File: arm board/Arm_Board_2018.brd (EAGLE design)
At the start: 193.8 x 103.9 mm, 165 parts, among them J1 RJ45KEYSTONE-942, J10 APP_2POS_CONFIGGENERAL_CONFIG, J11 APP_2POS_CONFIGGENERAL_CONFIG, J12 APP_2POS_CONFIGGENERAL_CONFIG, J13 APP_2POS_CONFIGGENERAL_CONFIG, J14 SL02, J15 SL02, J16 SL02, J2 JTAG_ARM_10PIN, J4 SL02, J5 APP_2POS_CONFIGGENERAL_CONFIG, J6 APP_2POS_CONFIGGENERAL_CONFIG, J7 APP_2POS_CONFIGGENERAL_CONFIG, J9 APP_2POS_CONFIGGENERAL_CONFIG, Q1 Q_IRF7437SMD, U1 TM4C1294NCPDT, U2 HX1198FNL, U3 SLVU2.8-4, Y1 NX3225GA, Y2 CRYATL_32K_SMD

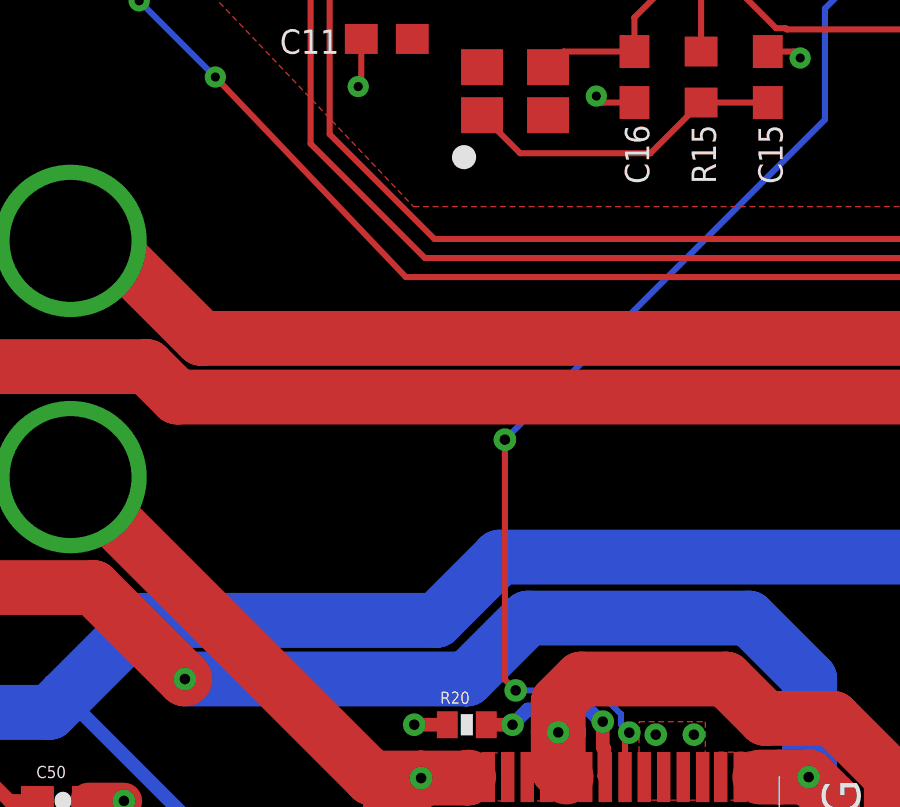
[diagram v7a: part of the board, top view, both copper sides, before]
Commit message: Connected the 3V3 plane to Logic 3.3V input
Fixed the fact that the tiva would not have any power without connecting
to the logic line.
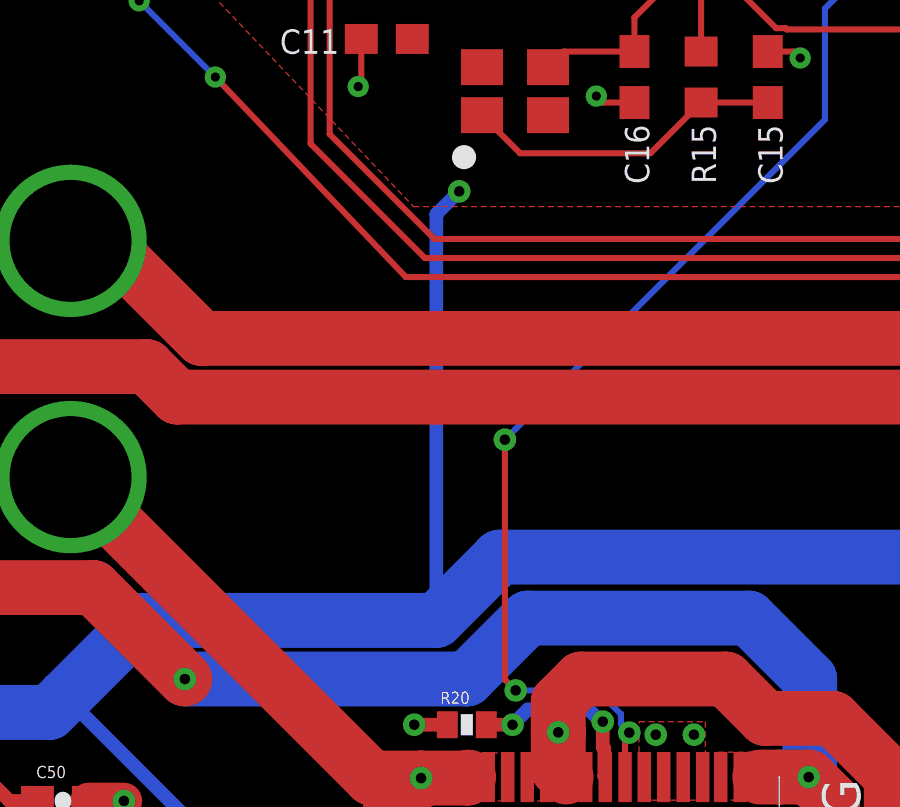
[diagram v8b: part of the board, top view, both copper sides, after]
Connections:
- removed net +3V3: C1.1, C10.1, C11.1, C2.1, C3.1, C4.1, C8.1, C9.1, J2.P1, LED3.A, R1.1, R12.2, R13.2, R17.1, R2.1, R3.1, R4.1, U1.P$101, U1.P$113, U1.P$122, U1.P$16, U1.P$26, U1.P$28, U1.P$39, U1.P$47, U1.P$51, U1.P$52, U1.P$69, U1.P$7, U1.P$79, U1.P$8, U1.P$9, U1.P$90, U2.P$2, U2.P$7
- net LOGIC_3.3V: now also C1.1, C10.1, C11.1, C2.1, C3.1, C4.1, C8.1, C9.1, J2.P1, LED3.A, R1.1, R12.2, R13.2, R17.1, R2.1, R3.1, R4.1, U1.P$101, U1.P$113, U1.P$122, U1.P$16, U1.P$26, U1.P$28, U1.P$39, U1.P$47, U1.P$51, U1.P$52, U1.P$69, U1.P$7, U1.P$79, U1.P$8, U1.P$9, U1.P$90, U2.P$2, U2.P$7
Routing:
- net LOGIC_3.3V: track 547.7 -> 569.0 mm, vias 14 -> 15
- net +3V3: track 9.27 -> 2.54 mm
- added copper zone on layer 1, net LOGIC_3.3V
- removed copper zone on layer 1, net +3V3
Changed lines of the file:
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@@
 <signals>
 <signal name="+3V3">
-<contactref element="U2" pad="P$2"/>
-<contactref element="C1" pad="1"/>
-<contactref element="R1" pad="1"/>
-<contactref element="R2" pad="1"/>
-<contactref element="R3" pad="1"/>
-<contactref element="R4" pad="1"/>
-<contactref element="C2" pad="1"/>
-<contactref element="C3" pad="1"/>
-<contactref element="R12" pad="2"/>
-<contactref element="R13" pad="2"/>
-<contactref element="U1" pad="P$9"/>
-<contactref element="U1" pad="P$7"/>
-<contactref element="U1" pad="P$122"/>
-<contactref element="U1" pad="P$113"/>
-<contactref element="U1" pad="P$101"/>
-<contactref element="U1" pad="P$90"/>
-<contactref element="U1" pad="P$79"/>
-<contactref element="U1" pad="P$69"/>
-<contactref element="U1" pad="P$52"/>
-<contactref element="U1" pad="P$51"/>
-<contactref element="U1" pad="P$47"/>
-<contactref element="U1" pad="P$39"/>
-<contactref element="U1" pad="P$28"/>
-<contactref element="U1" pad="P$26"/>
-<contactref element="U1" pad="P$16"/>
-<contactref element="U1" pad="P$8"/>
-<contactref element="C8" pad="1"/>
-<contactref element="C9" pad="1"/>
-<contactref element="C10" pad="1"/>
-<contactref element="C11" pad="1"/>
-<contactref element="R17" pad="1"/>
-<contactref element="J2" pad="P1"/>
-<polygon width="0.2032" layer="1">
-<vertex x="35.052" y="79.248"/>
-<vertex x="35.052" y="69.977"/>
-<vertex x="28.067" y="63.246"/>
-<vertex x="28.067" y="51.181"/>
-<vertex x="37.846" y="40.894"/>
-<vertex x="66.802" y="40.894"/>
-<vertex x="66.548" y="70.612"/>
-<vertex x="59.944" y="79.248"/>
-</polygon>
-<contactref element="C4" pad="1"/>
-<contactref element="U2" pad="P$7"/>
 <via x="46.482" y="68.707" extent="1-16" drill="0.3048"/>
 <via x="43.942" y="68.707" extent="1-16" drill="0.3048"/>
 <wire x1="43.942" y1="68.707" x2="46.482" y2="68.707" width="0.2032" layer="16"/>
-<contactref element="LED3" pad="A"/>
-<wire x1="46.97603125" y1="64.128953125" x2="46.97603125" y2="64.08546875" width="0.2032" layer="1"/>
-<wire x1="46.97603125" y1="64.08546875" x2="47.752" y2="63.3095" width="0.2032" layer="1"/>
-<wire x1="60.72925625" y1="62.714740625" x2="60.809740625" y2="62.714740625" width="0.2032" layer="1"/>
-<wire x1="60.809740625" y1="62.714740625" x2="61.722" y2="63.627" width="0.2032" layer="1"/>
-<wire x1="60.809740625" y1="62.714740625" x2="59.817" y2="61.722" width="0.2032" layer="1"/>
-<wire x1="66.968" y1="72.898" x2="64.516" y2="72.898" width="0.2032" layer="1"/>
-<wire x1="64.516" y1="72.898" x2="64.262" y2="72.644" width="0.2032" layer="1"/>
 </signal>
 <signal name="GND">
@@
 <via x="65.024" y="30.734" extent="1-16" drill="0.35"/>
 <wire x1="70.866" y1="23.114" x2="65.024" y2="28.956" width="0.4572" layer="1"/>
+<wire x1="38.608" y1="27.1018" x2="38.608" y2="40.64" width="0.4572" layer="16"/>
+<wire x1="38.608" y1="40.64" x2="39.37" y2="41.402" width="0.4572" layer="16"/>
+<via x="39.37" y="41.402" extent="1-16" drill="0.35"/>
+<contactref element="R12" pad="2"/>
+<contactref element="R13" pad="2"/>
+<contactref element="U1" pad="P$9"/>
+<contactref element="U1" pad="P$7"/>
+<contactref element="U1" pad="P$122"/>
+<contactref element="U1" pad="P$113"/>
+<contactref element="U1" pad="P$101"/>
+<contactref element="U1" pad="P$90"/>
+<contactref element="U1" pad="P$79"/>
+<contactref element="U1" pad="P$69"/>
+<contactref element="U1" pad="P$52"/>
+<contactref element="U1" pad="P$51"/>
+<contactref element="U1" pad="P$47"/>
+<contactref element="U1" pad="P$39"/>
+<contactref element="U1" pad="P$28"/>
+<contactref element="U1" pad="P$26"/>
+<contactref element="U1" pad="P$16"/>
+<contactref element="U1" pad="P$8"/>
+<contactref element="C8" pad="1"/>
+<contactref element="C9" pad="1"/>
+<contactref element="C10" pad="1"/>
+<contactref element="C11" pad="1"/>
+<wire x1="46.97603125" y1="64.128953125" x2="46.97603125" y2="64.08546875" width="0.2032" layer="1"/>
+<wire x1="46.97603125" y1="64.08546875" x2="47.752" y2="63.3095" width="0.2032" layer="1"/>
+<wire x1="60.72925625" y1="62.714740625" x2="60.809740625" y2="62.714740625" width="0.2032" layer="1"/>
+<wire x1="60.809740625" y1="62.714740625" x2="61.722" y2="63.627" width="0.2032" layer="1"/>
+<wire x1="60.809740625" y1="62.714740625" x2="59.817" y2="61.722" width="0.2032" layer="1"/>
+<wire x1="66.968" y1="72.898" x2="64.516" y2="72.898" width="0.2032" layer="1"/>
+<wire x1="64.516" y1="72.898" x2="64.262" y2="72.644" width="0.2032" layer="1"/>
+<contactref element="R17" pad="1"/>
+<contactref element="LED3" pad="A"/>
+<contactref element="J2" pad="P1"/>
+<contactref element="U2" pad="P$2"/>
+<contactref element="C1" pad="1"/>
+<contactref element="R1" pad="1"/>
+<contactref element="R2" pad="1"/>
+<contactref element="R3" pad="1"/>
+<contactref element="R4" pad="1"/>
+<contactref element="C2" pad="1"/>
+<contactref element="C3" pad="1"/>
+<contactref element="C4" pad="1"/>
+<contactref element="U2" pad="P$7"/>
+<polygon width="0.2032" layer="1">
+<vertex x="35.052" y="79.248"/>
+<vertex x="35.052" y="69.977"/>
+<vertex x="28.067" y="63.246"/>
+<vertex x="28.067" y="51.181"/>
+<vertex x="37.846" y="40.894"/>
+<vertex x="66.802" y="40.894"/>
+<vertex x="66.548" y="70.612"/>
+<vertex x="59.944" y="79.248"/>
+</polygon>
 </signal>
 <signal name="MOTOR1_2">
